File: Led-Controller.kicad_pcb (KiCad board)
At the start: 2 copper layers, 64.8 x 49.8 mm, 43 parts, among them J1 Screw_Terminal_01x06, J2 Barrel_Jack_Switch_Pin3Ring, Q1 CSD18540Q5B, Q2 CSD18540Q5B, Q3 CSD18540Q5B, Q4 CSD18540Q5B, Q5 CSD18540Q5B, U1 1ED44175N01BXTSA1, U2 AMS1117-5.0, U3 AMS1117-3.3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

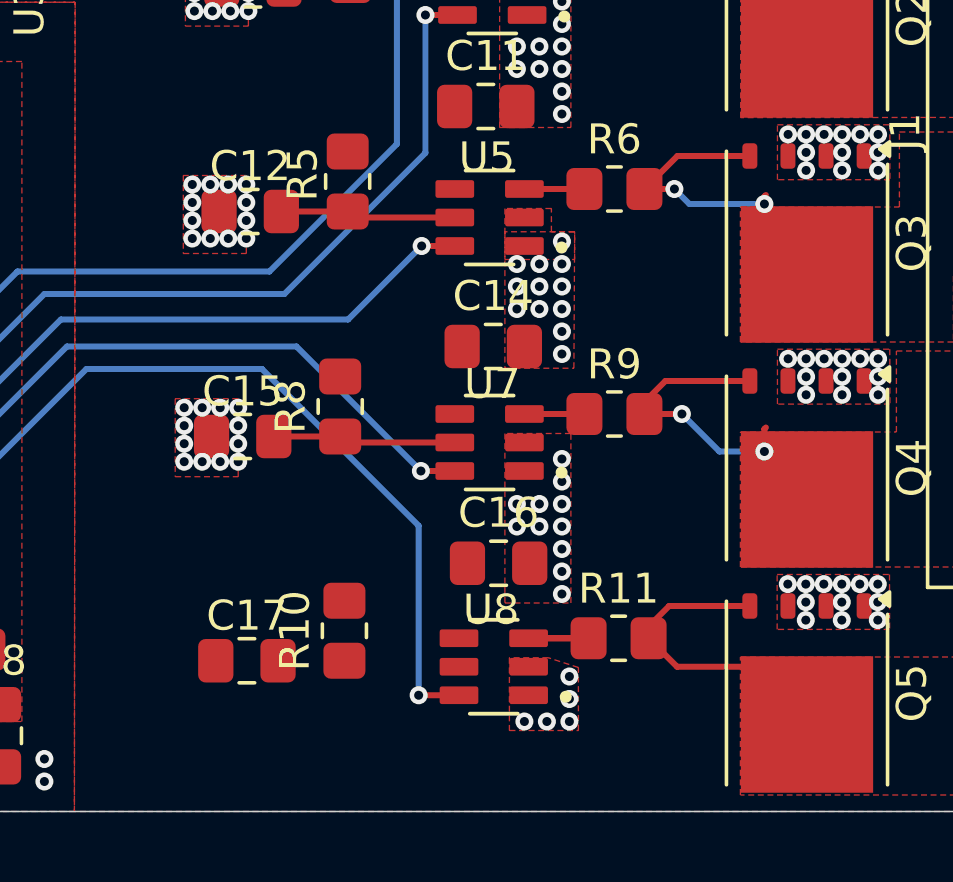
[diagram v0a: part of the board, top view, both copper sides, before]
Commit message: Fixed: Missing trace of RC circuit connecting to the gate driver (#17)
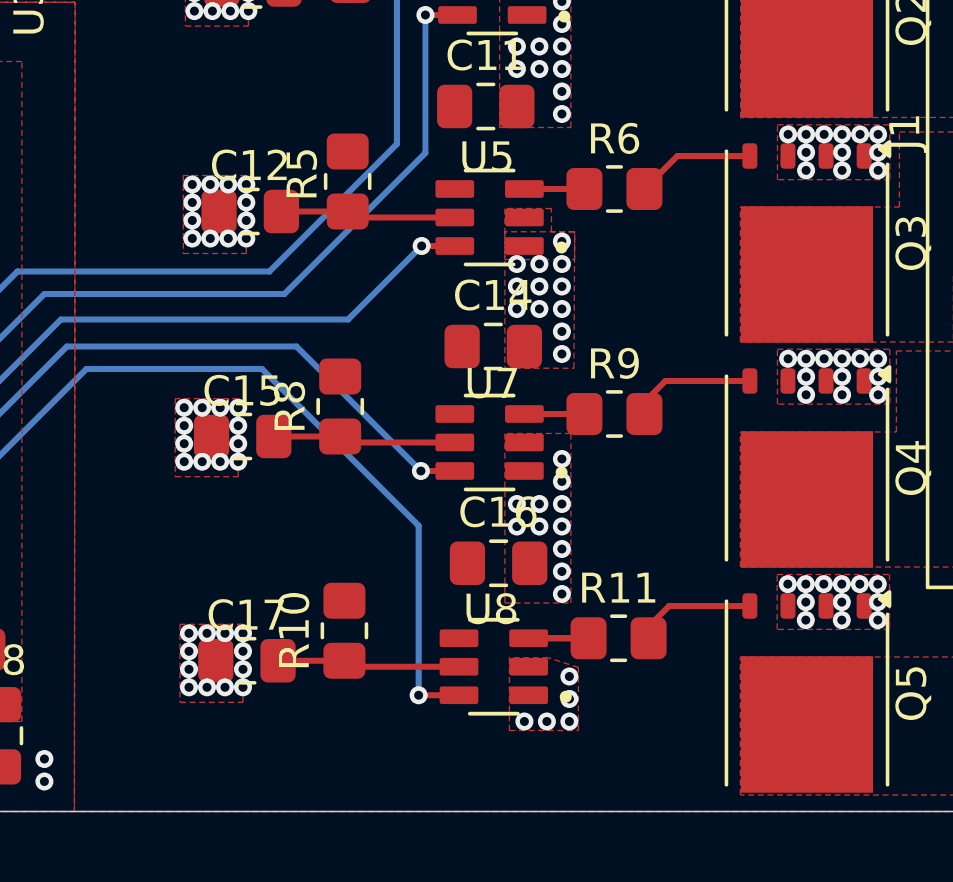
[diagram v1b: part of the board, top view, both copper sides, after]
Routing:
- net Net-(U8-EN/~{FLT}): track 0.00 -> 6.12 mm
- net /IN2: track 33.7 -> 28.4 mm, vias 4 -> 2
- net Net-(U5-OUT): track 6.53 -> 2.00 mm, vias 2 -> 0
- net /IN4: track 28.1 -> 23.8 mm
- net Net-(U8-OUT): track 2.00 -> 4.00 mm
- net Net-(U7-OUT): track 2.00 -> 4.00 mm
- net /IN3: track 24.9 -> 22.9 mm
- net /IN1: track 36.7 -> 34.7 mm
- net GND: vias 235 -> 247
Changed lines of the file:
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@@
+	)
+	(via
+		(at 105.12 133.01)
+		(size 0.6)
+		(drill 0.3)
+		(layers "F.Cu" "B.Cu")
+		(free yes)
+		(net 1)
 	)
 	(via
@@
 	)
 	(via
+		(at 105.12 131.81)
+		(size 0.6)
+		(drill 0.3)
+		(layers "F.Cu" "B.Cu")
+		(free yes)
+		(net 1)
+	)
+	(via
 		(at 114.25 105)
 		(size 0.6)
@@
 	)
 	(via
+		(at 103.32 131.81)
+		(size 0.6)
+		(drill 0.3)
+		(layers "F.Cu" "B.Cu")
+		(free yes)
+		(net 1)
+	)
+	(via
 		(at 125.09 123.26)
 		(size 0.6)
@@
 	)
 	(via
+		(at 103.32 133.01)
+		(size 0.6)
+		(drill 0.3)
+		(layers "F.Cu" "B.Cu")
+		(free yes)
+		(net 1)
+	)
+	(via
 		(at 115 120.25)
 		(size 0.6)
@@
 	)
 	(via
+		(at 103.92 131.81)
+		(size 0.6)
+		(drill 0.3)
+		(layers "F.Cu" "B.Cu")
+		(free yes)
+		(net 1)
+	)
+	(via
 		(at 90 103.2)
 		(size 0.6)
@@
 	)
 	(via
+		(at 104.52 131.81)
+		(size 0.6)
+		(drill 0.3)
+		(layers "F.Cu" "B.Cu")
+		(free yes)
+		(net 1)
+	)
+	(via
 		(at 105.3 111.07)
 		(size 0.6)
@@
 	)
 	(via
+		(at 105.12 133.61)
+		(size 0.6)
+		(drill 0.3)
+		(layers "F.Cu" "B.Cu")
+		(free yes)
+		(net 1)
+	)
+	(via
 		(at 126.19 100.77)
 		(size 0.6)
@@
 	)
 	(via
+		(at 103.92 133.61)
+		(size 0.6)
+		(drill 0.3)
+		(layers "F.Cu" "B.Cu")
+		(free yes)
+		(net 1)
+	)
+	(via
 		(at 104.96 124.29)
 		(size 0.6)
@@
 	)
 	(via
+		(at 103.32 133.61)
+		(size 0.6)
+		(drill 0.3)
+		(layers "F.Cu" "B.Cu")
+		(free yes)
+		(net 1)
+	)
+	(via
 		(at 103.5 101.75)
 		(size 0.6)
@@
 	)
 	(via
+		(at 105.12 132.41)
+		(size 0.6)
+		(drill 0.3)
+		(layers "F.Cu" "B.Cu")
+		(free yes)
+		(net 1)
+	)
+	(via
 		(at 125.08 130.77)
 		(size 0.6)
@@
 	)
 	(via
+		(at 104.52 133.61)
+		(size 0.6)
+		(drill 0.3)
+		(layers "F.Cu" "B.Cu")
+		(free yes)
+		(net 1)
+	)
+	(via
 		(at 84.2 103.8)
 		(size 0.6)
@@
 	(via
 		(at 103.43 118.05)
+		(size 0.6)
+		(drill 0.3)
+		(layers "F.Cu" "B.Cu")
+		(free yes)
+		(net 1)
+	)
+	(via
+		(at 103.32 132.41)
 		(size 0.6)
 		(drill 0.3)
@@
 	)
 	(segment
+		(start 108.7 132.925)
+		(end 108.5 132.725)
+		(width 0.2)
+		(layer "F.Cu")
+		(net 7)
+	)
+	(segment
+		(start 112.32 132.925)
+		(end 108.7 132.925)
+		(width 0.2)
+		(layer "F.Cu")
+		(net 7)
+	)
+	(segment
+		(start 106.2875 132.725)
+		(end 108.5 132.725)
+		(width 0.2)
+		(layer "F.Cu")
+		(net 7)
+	)
+	(segment
 		(start 119.6 100.9)
 		(end 121.93 100.9)
@@
 		(layer "F.Cu")
 		(net 10)
+	)
+	(segment
+		(start 114.5 124.5)
+		(end 116.5 124.5)
+		(width 0.2)
+		(layer "F.Cu")
+		(net 10)
+	)
+	(segment
+		(start 114.64 131.975)
+		(end 116.64 131.975)
+		(width 0.2)
+		(layer "F.Cu")
+		(net 11)
 	)
 	(segment
@@
 		(layer "F.Cu")
 		(net 15)
-	)
-	(segment
-		(start 118.5 117)
-		(end 119.5 117)
-		(width 0.2)
-		(layer "F.Cu")
-		(net 15)
-	)
-	(segment
-		(start 122.5 117.25)
-		(end 122.55 117.2)
-		(width 0.2)
-		(layer "F.Cu")
-		(net 15)
-	)
-	(segment
-		(start 122.5 117.5)
-		(end 122.5 117.25)
-		(width 0.2)
-		(layer "F.Cu")
-		(net 15)
-	)
-	(via
-		(at 122.5 117.5)
-		(size 0.6)
-		(drill 0.3)
-		(layers "F.Cu" "B.Cu")
-		(net 15)
-	)
-	(via
-		(at 119.5 117)
-		(size 0.6)
-		(drill 0.3)
-		(layers "F.Cu" "B.Cu")
-		(net 15)
-	)
-	(segment
-		(start 120 117.5)
-		(end 119.5 117)
-		(width 0.2)
-		(layer "B.Cu")
-		(net 15)
-	)
-	(segment
-		(start 122.5 117.5)
-		(end 120 117.5)
-		(width 0.2)
-		(layer "B.Cu")
-		(net 15)
-	)
-	(segment
-		(start 114.5 124.5)
-		(end 116.5 124.5)
-		(width 0.2)
-		(layer "F.Cu")
-		(net 16)
-	)
-	(segment
-		(start 118.5 124.5)
-		(end 119.75 124.5)
-		(width 0.2)
-		(layer "F.Cu")
-		(net 17)
-	)
-	(segment
-		(start 122.5 125.75)
-		(end 122.5 125)
-		(width 0.2)
-		(layer "F.Cu")
-		(net 17)
-	)
-	(segment
-		(start 122.5 125)
-		(end 122.55 124.95)
-		(width 0.2)
-		(layer "F.Cu")
-		(net 17)
-	)
-	(via
-		(at 119.75 124.5)
-		(size 0.6)
-		(drill 0.3)
-		(layers "F.Cu" "B.Cu")
-		(net 17)
-	)
-	(via
-		(at 122.5 125.75)
-		(size 0.6)
-		(drill 0.3)
-		(layers "F.Cu" "B.Cu")
-		(net 17)
-	)
-	(segment
-		(start 121 125.75)
-		(end 122.5 125.75)
-		(width 0.2)
-		(layer "B.Cu")
-		(net 17)
-	)
-	(segment
-		(start 119.75 124.5)
-		(end 121 125.75)
-		(width 0.2)
-		(layer "B.Cu")
-		(net 17)
-	)
-	(segment
-		(start 114.64 131.975)
-		(end 116.64 131.975)
-		(width 0.2)
-		(layer "F.Cu")
-		(net 18)
-	)
-	(segment
-		(start 118.64 131.975)
-		(end 119.59 132.925)
-		(width 0.2)
-		(layer "F.Cu")
-		(net 19)
-	)
-	(segment
-		(start 119.59 132.925)
-		(end 122.55 132.925)
-		(width 0.2)
-		(layer "F.Cu")
-		(net 19)
 	)
 	(segment
@@
 			)
 		)
+	)
+	(zone
+		(net 1)
+		(net_name "GND")
+		(layer "F.Cu")
+		(hatch edge 0.5)
+		(priority 8)
+		(connect_pads
+			(clearance 0.5)
+		)
+		(min_thickness 0.25)
+		(filled_areas_thickness no)
+		(fill yes
+			(thermal_gap 0.25)
+			(thermal_bridge_width 0.3)
+		)
+		(polygon
+			(pts
+				(xy 105.12 131.51) (xy 103.02 131.51) (xy 103.02 134.11) (xy 105.12 134.11)
+			)
+		)
